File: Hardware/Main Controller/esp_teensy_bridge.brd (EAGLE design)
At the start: 102.8 x 87.9 mm, 42 parts, among them IC1 BQ79600PWRQ1, Q1 SI7611DN-T1-GE3, Q2 SI7611DN-T1-GE3, Q3 SI7611DN-T1-GE3, Q4 SI7611DN-T1-GE3

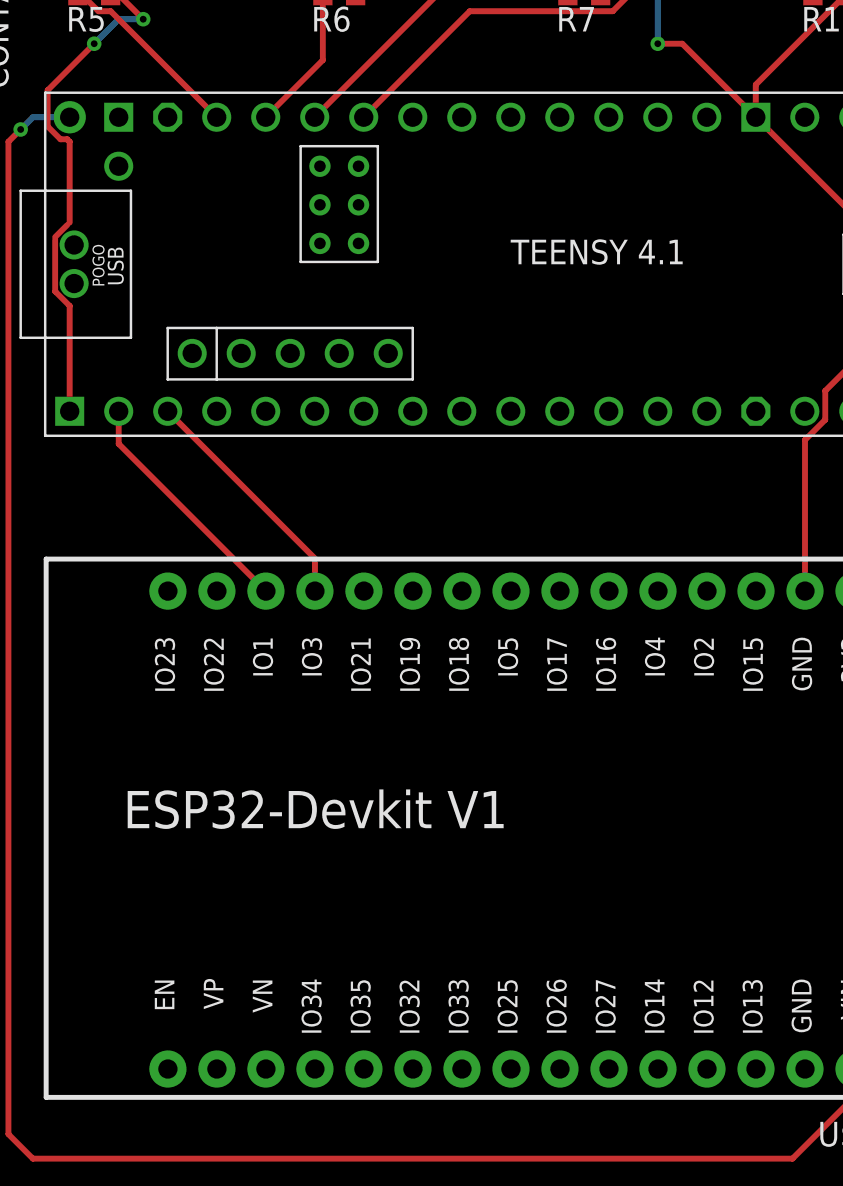
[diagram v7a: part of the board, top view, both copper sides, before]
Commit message: change from uart to spi
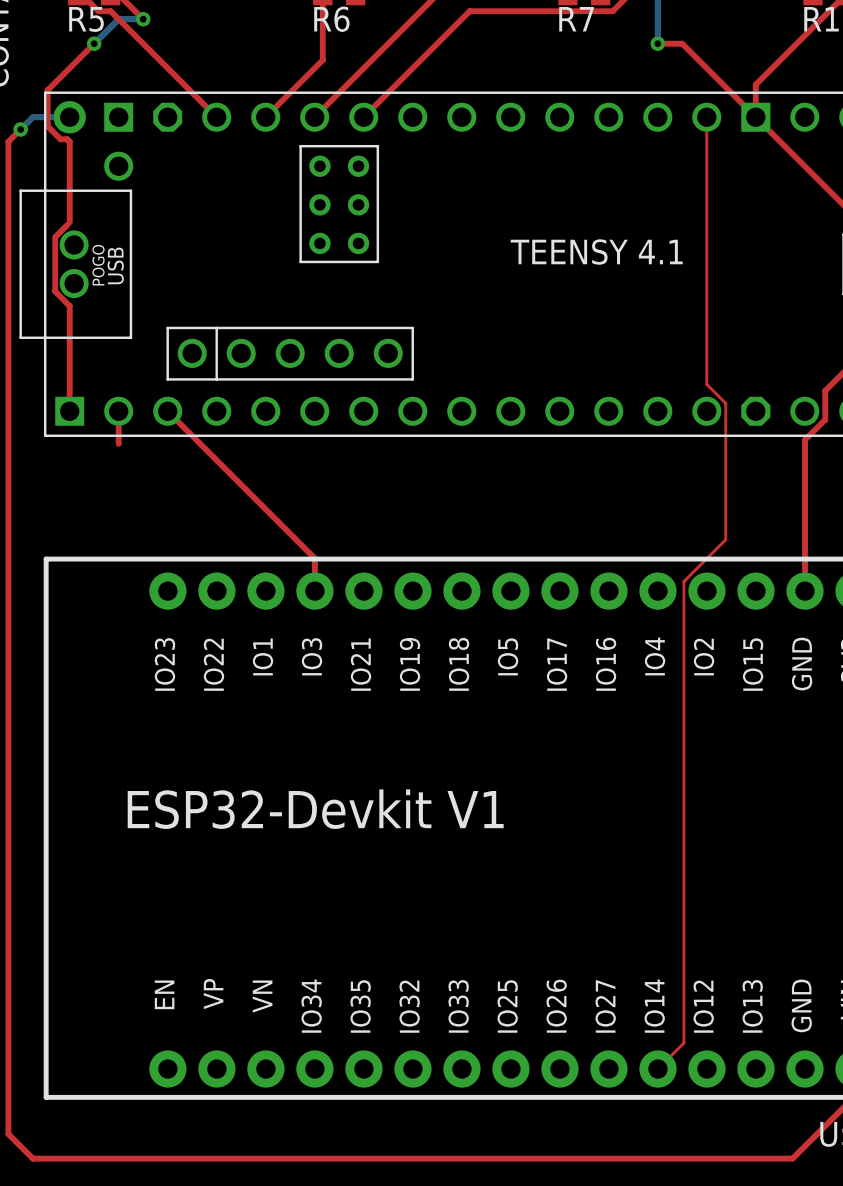
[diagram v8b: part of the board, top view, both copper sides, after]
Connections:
- new net CS0: IC1.7, U$3.38-A14/CS/IN1
- new net CS1: U$2.3, U$3.39-A15/CS/OUT1A
- new net CS2: U$3.40-A16/CS1
- new net MISO: IC1.5, U$2.27, U$3.12-MISO/MQSL
- new net MOSI: IC1.4, U$2.28, U$3.11-MOSI/CTX1
- new net SCK: IC1.6, U$2.26, U$3.13-SCK/LED
- net GND: no longer IC1.6, IC1.7
- net RX_BRIDGE: no longer IC1.4
- net RX_ESP: no longer U$2.12
- net TX_BRIDGE: no longer IC1.5
- net TX_ESP: no longer U$2.13
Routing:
- net SCK: track 0.00 -> 51.2 mm
- net TX_ESP: track 12.5 -> 1.69 mm
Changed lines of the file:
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@@
 <contactref element="C3" pad="1"/>
 <contactref element="R8" pad="2"/>
-<contactref element="IC1" pad="6"/>
 <contactref element="IC1" pad="8"/>
-<contactref element="IC1" pad="7"/>
 <contactref element="TME1205S" pad="1"/>
 <contactref element="C4" pad="2"/>
@@
 <wire x1="68.795" y1="41.91" x2="64.35" y2="41.91" width="0" layer="19" extent="1-1"/>
 <wire x1="68.182" y1="35.915" x2="68.795" y2="41.91" width="0" layer="19" extent="1-1"/>
-<wire x1="68.182" y1="33.315" x2="68.182" y2="35.915" width="0" layer="19" extent="1-1"/>
-<wire x1="68.182" y1="32.665" x2="68.182" y2="33.315" width="0" layer="19" extent="1-1"/>
-<wire x1="68.182" y1="32.015" x2="68.182" y2="32.665" width="0" layer="19" extent="1-1"/>
+<wire x1="68.182" y1="32.015" x2="68.182" y2="35.915" width="0" layer="19" extent="1-1"/>
 <wire x1="74.058" y1="32.015" x2="68.182" y2="32.015" width="0" layer="19" extent="1-1"/>
 <wire x1="59.055" y1="36.83" x2="64.35" y2="41.91" width="0" layer="19" extent="1-1"/>
@@
 </signal>
 <signal name="TX_ESP">
-<contactref element="U$2" pad="13"/>
 <contactref element="U$3" pad="0-RX1/CS1/CRX2"/>
-<wire x1="15.25" y1="49.735" x2="7.62" y2="57.365" width="0.3048" layer="1"/>
 <wire x1="7.62" y1="57.365" x2="7.62" y2="59.055" width="0.3048" layer="1"/>
 </signal>
 <signal name="RX_ESP">
-<contactref element="U$2" pad="12"/>
 <contactref element="U$3" pad="1-TX1/MISO1/CTX2"/>
-<wire x1="17.79" y1="50.165" x2="17.79" y2="49.735" width="0.1524" layer="1"/>
 <wire x1="10.16" y1="59.055" x2="17.79" y2="51.425" width="0.3048" layer="1"/>
 <wire x1="17.79" y1="51.425" x2="17.79" y2="50.165" width="0.3048" layer="1"/>
 </signal>
 <signal name="TX_BRIDGE">
-<contactref element="IC1" pad="5"/>
 <contactref element="U$3" pad="28-RX7"/>
-<wire x1="68.182" y1="33.965" x2="53.34" y2="59.055" width="0" layer="19" extent="1-1"/>
 </signal>
 <signal name="RX_BRIDGE">
-<contactref element="IC1" pad="4"/>
 <contactref element="U$3" pad="29-TX7"/>
-<wire x1="68.182" y1="34.615" x2="55.88" y2="59.055" width="0" layer="19" extent="1-1"/>
 </signal>
 <signal name="5V">
@@
 <wire x1="60.96" y1="59.055" x2="66.87" y2="54.82" width="0" layer="19" extent="1-1"/>
 </signal>
+<signal name="MOSI">
+<contactref element="IC1" pad="4"/>
+<contactref element="U$3" pad="11-MOSI/CTX1"/>
+<contactref element="U$2" pad="28"/>
+<wire x1="40.65" y1="24.965" x2="68.182" y2="34.615" width="0" layer="19" extent="1-1"/>
+<wire x1="35.56" y1="59.055" x2="40.65" y2="24.965" width="0" layer="19" extent="1-1"/>
+</signal>
+<signal name="MISO">
+<contactref element="IC1" pad="5"/>
+<contactref element="U$3" pad="12-MISO/MQSL"/>
+<contactref element="U$2" pad="27"/>
+<wire x1="38.11" y1="24.965" x2="68.182" y2="33.965" width="0" layer="19" extent="1-1"/>
+<wire x1="38.1" y1="59.055" x2="38.11" y2="24.965" width="0" layer="19" extent="1-1"/>
+</signal>
+<signal name="SCK">
+<contactref element="IC1" pad="6"/>
+<contactref element="U$3" pad="13-SCK/LED"/>
+<contactref element="U$2" pad="26"/>
+<wire x1="38.1" y1="74.295" x2="38.1" y2="60.44460625" width="0.1524" layer="1"/>
+<wire x1="38.1" y1="60.44460625" x2="39.0826" y2="59.46200625" width="0.1524" layer="1"/>
+<wire x1="36.9162" y1="26.3112" x2="35.57" y2="24.965" width="0.1524" layer="1"/>
+<wire x1="36.9162" y1="50.22949375" x2="36.9162" y2="26.3112" width="0.1524" layer="1"/>
+<wire x1="39.0826" y1="59.46200625" x2="39.0826" y2="52.39589375" width="0.1524" layer="1"/>
+<wire x1="39.0826" y1="52.39589375" x2="36.9162" y2="50.22949375" width="0.1524" layer="1"/>
+<wire x1="35.57" y1="24.965" x2="68.182" y2="33.315" width="0" layer="19" extent="1-1"/>
+</signal>
+<signal name="CS2">
+<contactref element="U$3" pad="40-A16/CS1"/>
+</signal>
+<signal name="CS1">
+<contactref element="U$3" pad="39-A15/CS/OUT1A"/>
+<contactref element="U$2" pad="3"/>
+<wire x1="40.65" y1="49.735" x2="48.26" y2="74.295" width="0" layer="19" extent="1-1"/>
+</signal>
+<signal name="CS0">
+<contactref element="U$3" pad="38-A14/CS/IN1"/>
+<contactref element="IC1" pad="7"/>
+<wire x1="68.182" y1="32.665" x2="50.8" y2="74.295" width="0" layer="19" extent="1-1"/>
+</signal>
 </signals>
